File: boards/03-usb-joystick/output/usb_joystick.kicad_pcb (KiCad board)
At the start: 2 copper layers, 80 x 60 mm, 19 parts, among them J1 USB-C, J2 Joystick, SW1 Button, SW2 Button, SW3 Button, SW4 Button, U1 MCU, Y1 16MHz

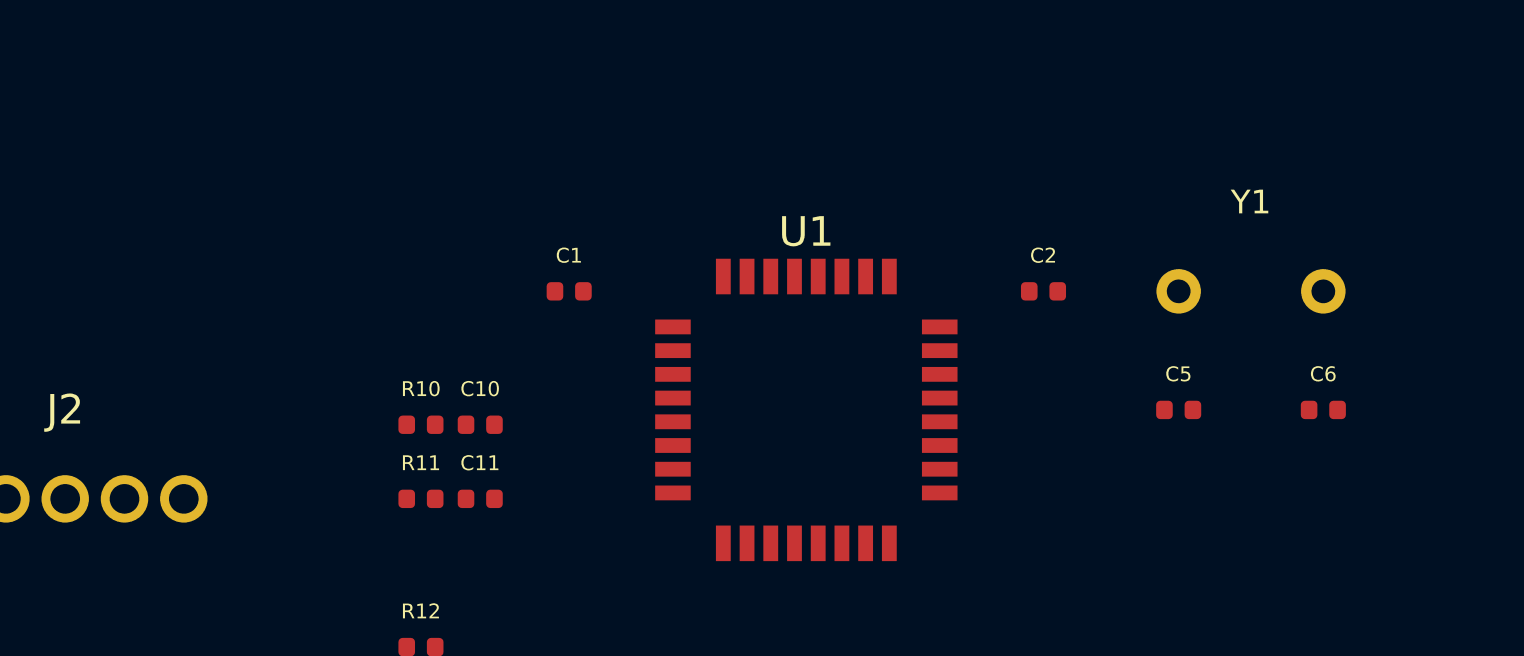
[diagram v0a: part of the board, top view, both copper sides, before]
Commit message: chore(board-03): fix crystal placement to west of MCU; reroute to 62% (8/13 nets)
Crystal Y1 was placed east of U1 (BOARD_ORIGIN_X+55) but MCU XTAL pins 2/3
are on the west edge of the TQFP-32. This created 17-22mm channel-blocked
routes across the MCU body. Move Y1 to BOARD_ORIGIN_X+22 (west, aligned with
U1 pin 2/3 at y≈30). Load caps C5/C6 follow. XTAL1 now fully routes (3/3 pads
complete). Overall routing: 42% baseline → 54% first pass → 62% after fix.
Remaining failures (USB_D+/D-, JOY_BTN, JOY_X, BTN1, XTAL2/Y1.2) documented
as channel-blocked in issues #2918 (crystal placement) and #2919 (USB-C pitch).

Co-Authored-By: Claude Sonnet 4.6 <noreply@anthropic.com>
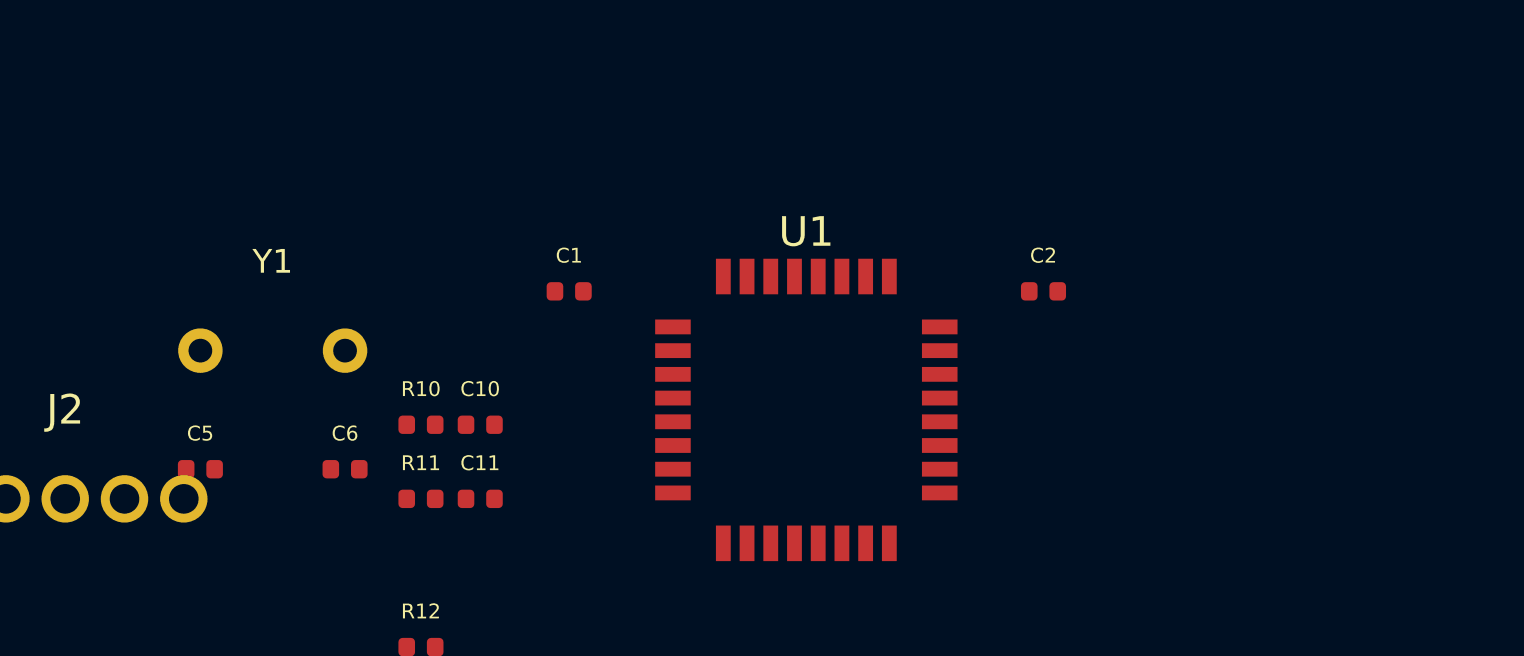
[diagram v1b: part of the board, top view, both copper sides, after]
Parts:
- moved C5 33.1 mm to (119.6, 134.0)
- moved C6 33.1 mm to (124.4, 134.0)
- moved Y1 33.1 mm to (122.0, 130.0)
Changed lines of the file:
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@@
   (footprint "Crystal:Crystal_HC49-U_Vertical"
     (layer "F.Cu")
-    (at 155.0 128.0)
+    (at 122.0 130.0)
     (fp_text reference "Y1" (at 0 -3) (layer "F.SilkS")
       (effects (font (size 0.8 0.8) (thickness 0.12)))
@@
   (footprint "Capacitor_SMD:C_0402_1005Metric"
     (layer "F.Cu")
-    (at 152.56 132.0)
+    (at 119.56 134.0)
     (fp_text reference "C5" (at 0 -1.2) (layer "F.SilkS")
       (effects (font (size 0.5 0.5) (thickness 0.1)))
@@
   (footprint "Capacitor_SMD:C_0402_1005Metric"
     (layer "F.Cu")
-    (at 157.44 132.0)
+    (at 124.44 134.0)
     (fp_text reference "C6" (at 0 -1.2) (layer "F.SilkS")
       (effects (font (size 0.5 0.5) (thickness 0.1)))

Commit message: wip(doctor): flip C5/C6 load caps north of Y1 to clear J2 collision
Source-level DRC check on the pre-route usb_joystick.kicad_pcb revealed
a -0.110mm pad-to-pad clearance violation: C5-1 (XTAL1 load-cap pad,
0.56 x 0.62 mm at (BOARD_ORIGIN_X + 19.08, BOARD_ORIGIN_Y + 34)) sits
directly on top of J2-5 (1.6 mm diameter through-hole pad at
(BOARD_ORIGIN_X + 19, BOARD_ORIGIN_Y + 35)).

Y1 crystal placement (BOARD_ORIGIN_X + 22, BOARD_ORIGIN_Y + 30, west of
U1's XTAL pad row) remains unchanged — that is the approved fix for
issue #2918. The load-cap downstream-offset (cap_dy = +4) inherits Y1's
new position and falls onto J2, which sits at y = 35 with TH pads
spanning x = 11..19.

Flip cap_dy to -4 (north of Y1 instead of south) so C5/C6 sit in the
empty area between Y1 (y = 30) and U1's north pad row (y = 27.5),
giving > 0.9 mm clearance on both sides. Source PCB now passes
pure-Python DRC at 0 errors, matching origin/main.

The routed PCB still needs regeneration in a follow-up commit.

Closes #2918

Co-Authored-By: Claude Opus 4.7 (1M context) <noreply@anthropic.com>
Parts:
- moved C5 8.00 mm to (119.6, 126.0)
- moved C6 8.00 mm to (124.4, 126.0)
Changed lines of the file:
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@@
   (footprint "Capacitor_SMD:C_0402_1005Metric"
     (layer "F.Cu")
-    (at 119.56 134.0)
+    (at 119.56 126.0)
     (fp_text reference "C5" (at 0 -1.2) (layer "F.SilkS")
       (effects (font (size 0.5 0.5) (thickness 0.1)))
@@
   (footprint "Capacitor_SMD:C_0402_1005Metric"
     (layer "F.Cu")
-    (at 124.44 134.0)
+    (at 124.44 126.0)
     (fp_text reference "C6" (at 0 -1.2) (layer "F.SilkS")
       (effects (font (size 0.5 0.5) (thickness 0.1)))
